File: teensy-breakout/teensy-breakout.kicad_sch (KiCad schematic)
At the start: 80 parts, among them J1 USB_B, J10 Conn_01x04, J11 Conn_01x04, J12 Conn_01x05, J13 Conn_01x03, J14 Conn_01x04, J15 Conn_01x04, J16 1988956, J17 Conn_01x08, J18 Conn_01x08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

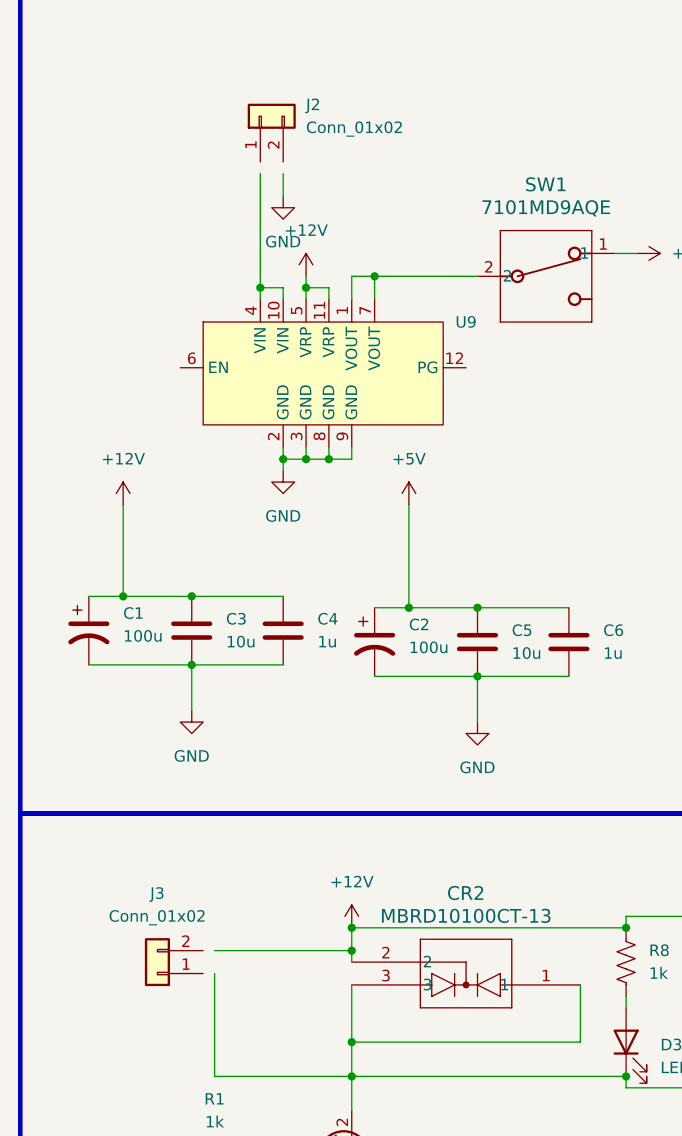
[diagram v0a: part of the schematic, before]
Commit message: Added footprints for connectors. Mostly JST, some XT30 and screw terminals.
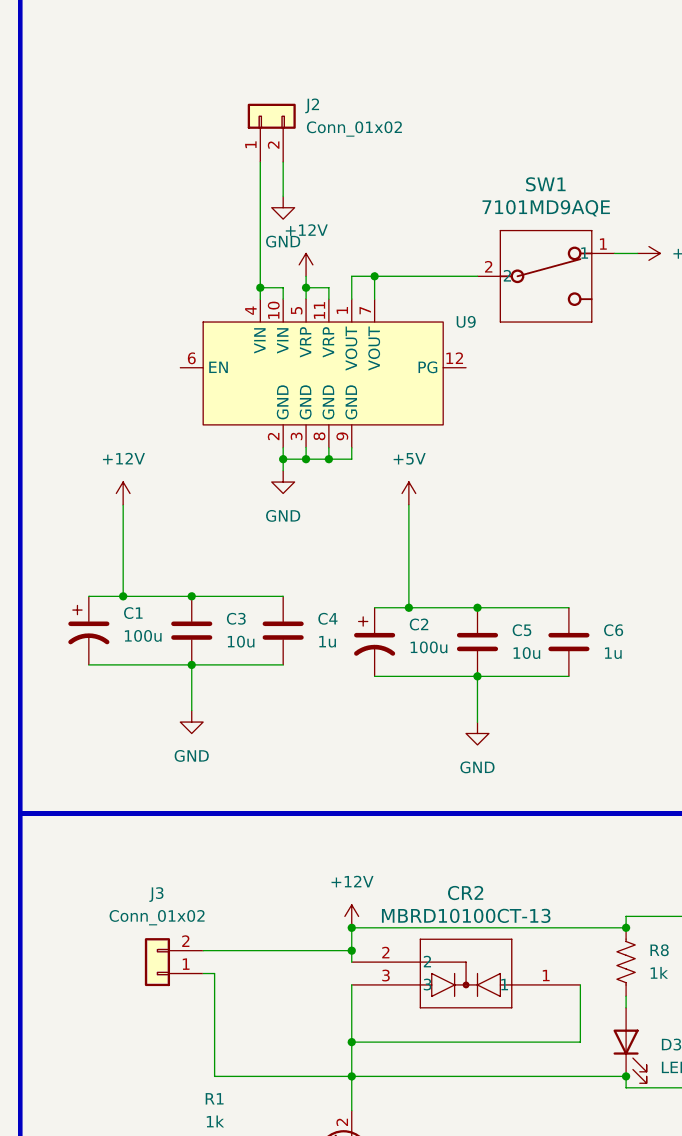
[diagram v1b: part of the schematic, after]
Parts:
- J10, J12, J4, J5, J6, J7, J8, J9: footprint (none) -> Connector_JST:JST_EH_B5B-EH-A_1x05_P2.50mm_Vertical
- J11, J14, J15: footprint (none) -> Connector_JST:JST_EH_B4B-EH-A_1x04_P2.50mm_Vertical
- J13, J19, J20, J21, J22: footprint (none) -> Connector_JST:JST_EH_B3B-EH-A_1x03_P2.50mm_Vertical
- J17, J18: footprint (none) -> Custom:PHOENIX_1989010
- J2, J3: footprint (none) -> Connector_AMASS:AMASS_XT60-F_1x02_P7.20mm_Vertical
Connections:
- net +12V: now also J3.2 (Pin_2)
- net GND: now also J2.2 (Pin_2)
- net at CR2.1, CR2.3, D3.1 (K)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: now also J3.1 (Pin_1)
- net at J2.1 (Pin_1): now also U9.10 (VIN), U9.4 (VIN)
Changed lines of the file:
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@@
 	(wire
 		(pts
-			(xy 33.02 121.92) (xy 48.26 121.92)
-		)
-		(stroke
-			(width 0)
-			(type default)
-		)
-	)
-	(wire
-		(pts
 			(xy 46.99 358.14) (xy 46.99 360.68)
 		)
@@
 	(wire
 		(pts
-			(xy 40.64 35.56) (xy 40.64 38.1)
-		)
-		(stroke
-			(width 0)
-			(type default)
-		)
-	)
-	(wire
-		(pts
 			(xy 218.44 299.72) (xy 219.71 299.72)
 		)
@@
 	(wire
 		(pts
+			(xy 31.75 121.92) (xy 48.26 121.92)
+		)
+		(stroke
+			(width 0)
+			(type default)
+		)
+	)
+	(wire
+		(pts
 			(xy 254 177.8) (xy 254 180.34)
 		)
@@
 	(wire
 		(pts
+			(xy 31.75 124.46) (xy 33.02 124.46)
+		)
+		(stroke
+			(width 0)
+			(type default)
+		)
+	)
+	(wire
+		(pts
 			(xy 341.63 190.5) (xy 350.52 190.5)
 		)
@@
 	(wire
 		(pts
+			(xy 40.64 34.29) (xy 40.64 38.1)
+		)
+		(stroke
+			(width 0)
+			(type default)
+		)
+	)
+	(wire
+		(pts
 			(xy 224.79 36.83) (xy 224.79 21.59)
 		)
@@
 	(wire
 		(pts
-			(xy 38.1 35.56) (xy 38.1 48.26)
+			(xy 38.1 34.29) (xy 38.1 48.26)
 		)
 		(stroke
@@
 			)
 		)
-		(property "Footprint" ""
+		(property "Footprint" "Connector_AMASS:AMASS_XT60-F_1x02_P7.20mm_Vertical"
 			(at 38.1 29.21 0)
 			(effects
@@
 			)
 		)
-		(property "Footprint" ""
+		(property "Footprint" "Connector_JST:JST_EH_B5B-EH-A_1x05_P2.50mm_Vertical"
 			(at 22.86 207.01 0)
 			(effects
@@
 			)
 		)
-		(property "Footprint" ""
+		(property "Footprint" "Connector_JST:JST_EH_B3B-EH-A_1x03_P2.50mm_Vertical"
 			(at 224.79 302.26 0)
 			(effects
@@
 			)
 		)
-		(property "Footprint" ""
+		(property "Footprint" "Connector_JST:JST_EH_B5B-EH-A_1x05_P2.50mm_Vertical"
 			(at 50.8 228.6 0)
 			(effects
@@
 			)
 		)
-		(property "Footprint" ""
+		(property "Footprint" "Connector_JST:JST_EH_B3B-EH-A_1x03_P2.50mm_Vertical"
 			(at 224.79 342.9 0)
 			(effects
@@
 			)
 		)
-		(property "Footprint" ""
+		(property "Footprint" "Custom:PHOENIX_1989010"
 			(at 306.07 81.28 0)
 			(effects
@@
 			)
 		)
-		(property "Footprint" ""
+		(property "Footprint" "Connector_JST:JST_EH_B5B-EH-A_1x05_P2.50mm_Vertical"
 			(at 22.86 184.15 0)
 			(effects
@@
 			)
 		)
-		(property "Footprint" ""
+		(property "Footprint" "Connector_JST:JST_EH_B5B-EH-A_1x05_P2.50mm_Vertical"
 			(at 207.01 182.88 0)
 			(effects
@@
 			)
 		)
-		(property "Footprint" ""
+		(property "Footprint" "Connector_JST:JST_EH_B5B-EH-A_1x05_P2.50mm_Vertical"
 			(at 50.8 207.01 0)
 			(effects
@@
 			)
 		)
-		(property "Footprint" ""
+		(property "Footprint" "Connector_JST:JST_EH_B4B-EH-A_1x04_P2.50mm_Vertical"
 			(at 318.77 60.96 0)
 			(effects
@@
 			)
 		)
-		(property "Footprint" ""
+		(property "Footprint" "Connector_JST:JST_EH_B3B-EH-A_1x03_P2.50mm_Vertical"
 			(at 318.77 35.56 0)
 			(effects
@@
 			)
 		)
-		(property "Footprint" ""
+		(property "Footprint" "Connector_JST:JST_EH_B4B-EH-A_1x04_P2.50mm_Vertical"
 			(at 318.77 48.26 0)
 			(effects
@@
 			)
 		)
-		(property "Footprint" ""
+		(property "Footprint" "Connector_JST:JST_EH_B3B-EH-A_1x03_P2.50mm_Vertical"
 			(at 224.79 322.58 0)
 			(effects
@@
 			)
 		)
-		(property "Footprint" ""
+		(property "Footprint" "Connector_AMASS:AMASS_XT60-F_1x02_P7.20mm_Vertical"
 			(at 26.67 124.46 0)
 			(effects
@@
 			)
 		)
-		(property "Footprint" ""
+		(property "Footprint" "Connector_JST:JST_EH_B5B-EH-A_1x05_P2.50mm_Vertical"
 			(at 106.68 292.1 0)
 			(effects
@@
 			)
 		)
-		(property "Footprint" ""
+		(property "Footprint" "Custom:PHOENIX_1989010"
 			(at 306.07 104.14 0)
 			(effects
@@
 			)
 		)
-		(property "Footprint" ""
+		(property "Footprint" "Connector_JST:JST_EH_B5B-EH-A_1x05_P2.50mm_Vertical"
 			(at 22.86 228.6 0)
 			(effects
@@
 			)
 		)
-		(property "Footprint" ""
+		(property "Footprint" "Connector_JST:JST_EH_B3B-EH-A_1x03_P2.50mm_Vertical"
 			(at 224.79 281.94 0)
 			(effects
@@
 			)
 		)
-		(property "Footprint" ""
+		(property "Footprint" "Connector_JST:JST_EH_B4B-EH-A_1x04_P2.50mm_Vertical"
 			(at 207.01 152.4 0)
 			(effects
@@
 			)
 		)
-		(property "Footprint" ""
+		(property "Footprint" "Connector_JST:JST_EH_B5B-EH-A_1x05_P2.50mm_Vertical"
 			(at 50.8 184.15 0)
 			(effects

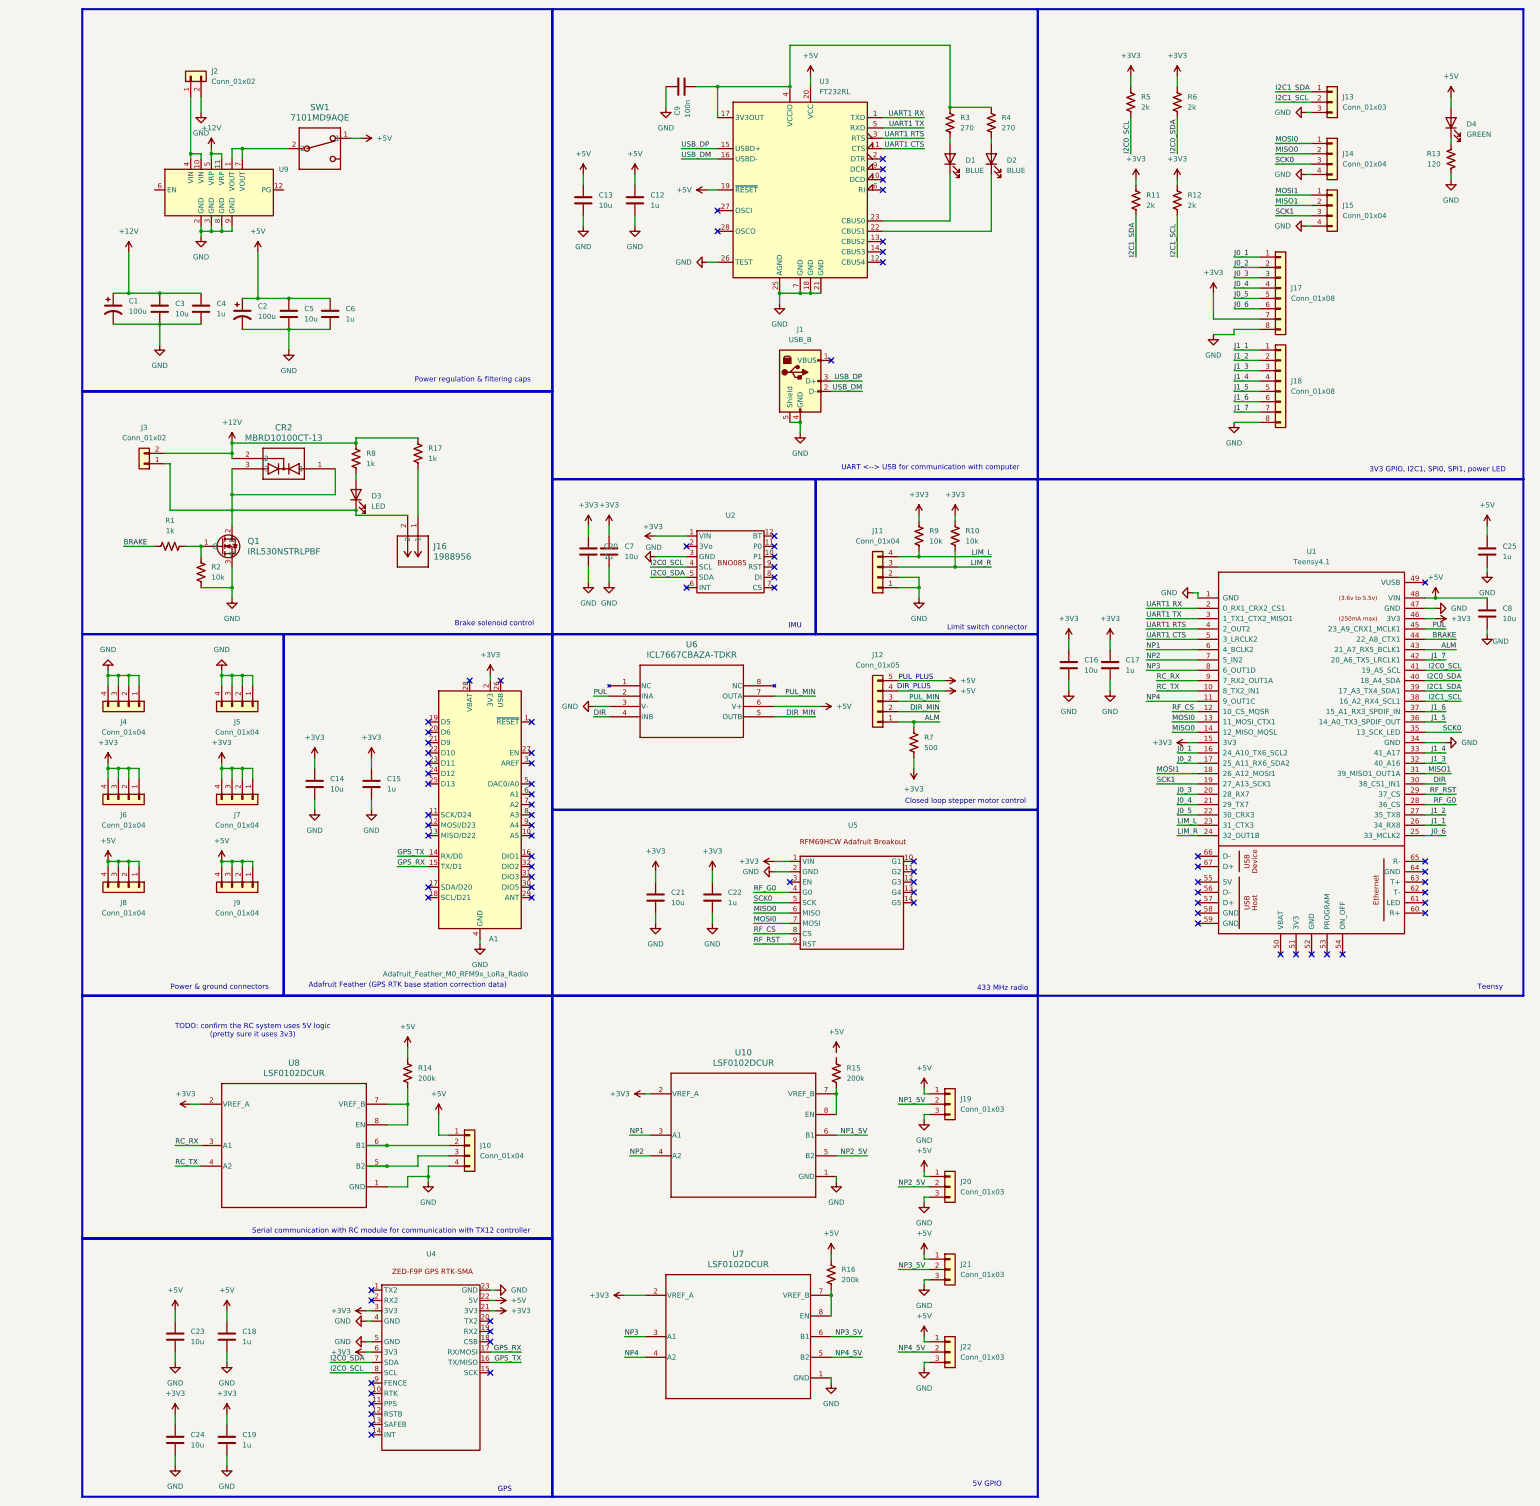
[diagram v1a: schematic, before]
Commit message: Did most of the routing, need to add pinouts and mounting holes
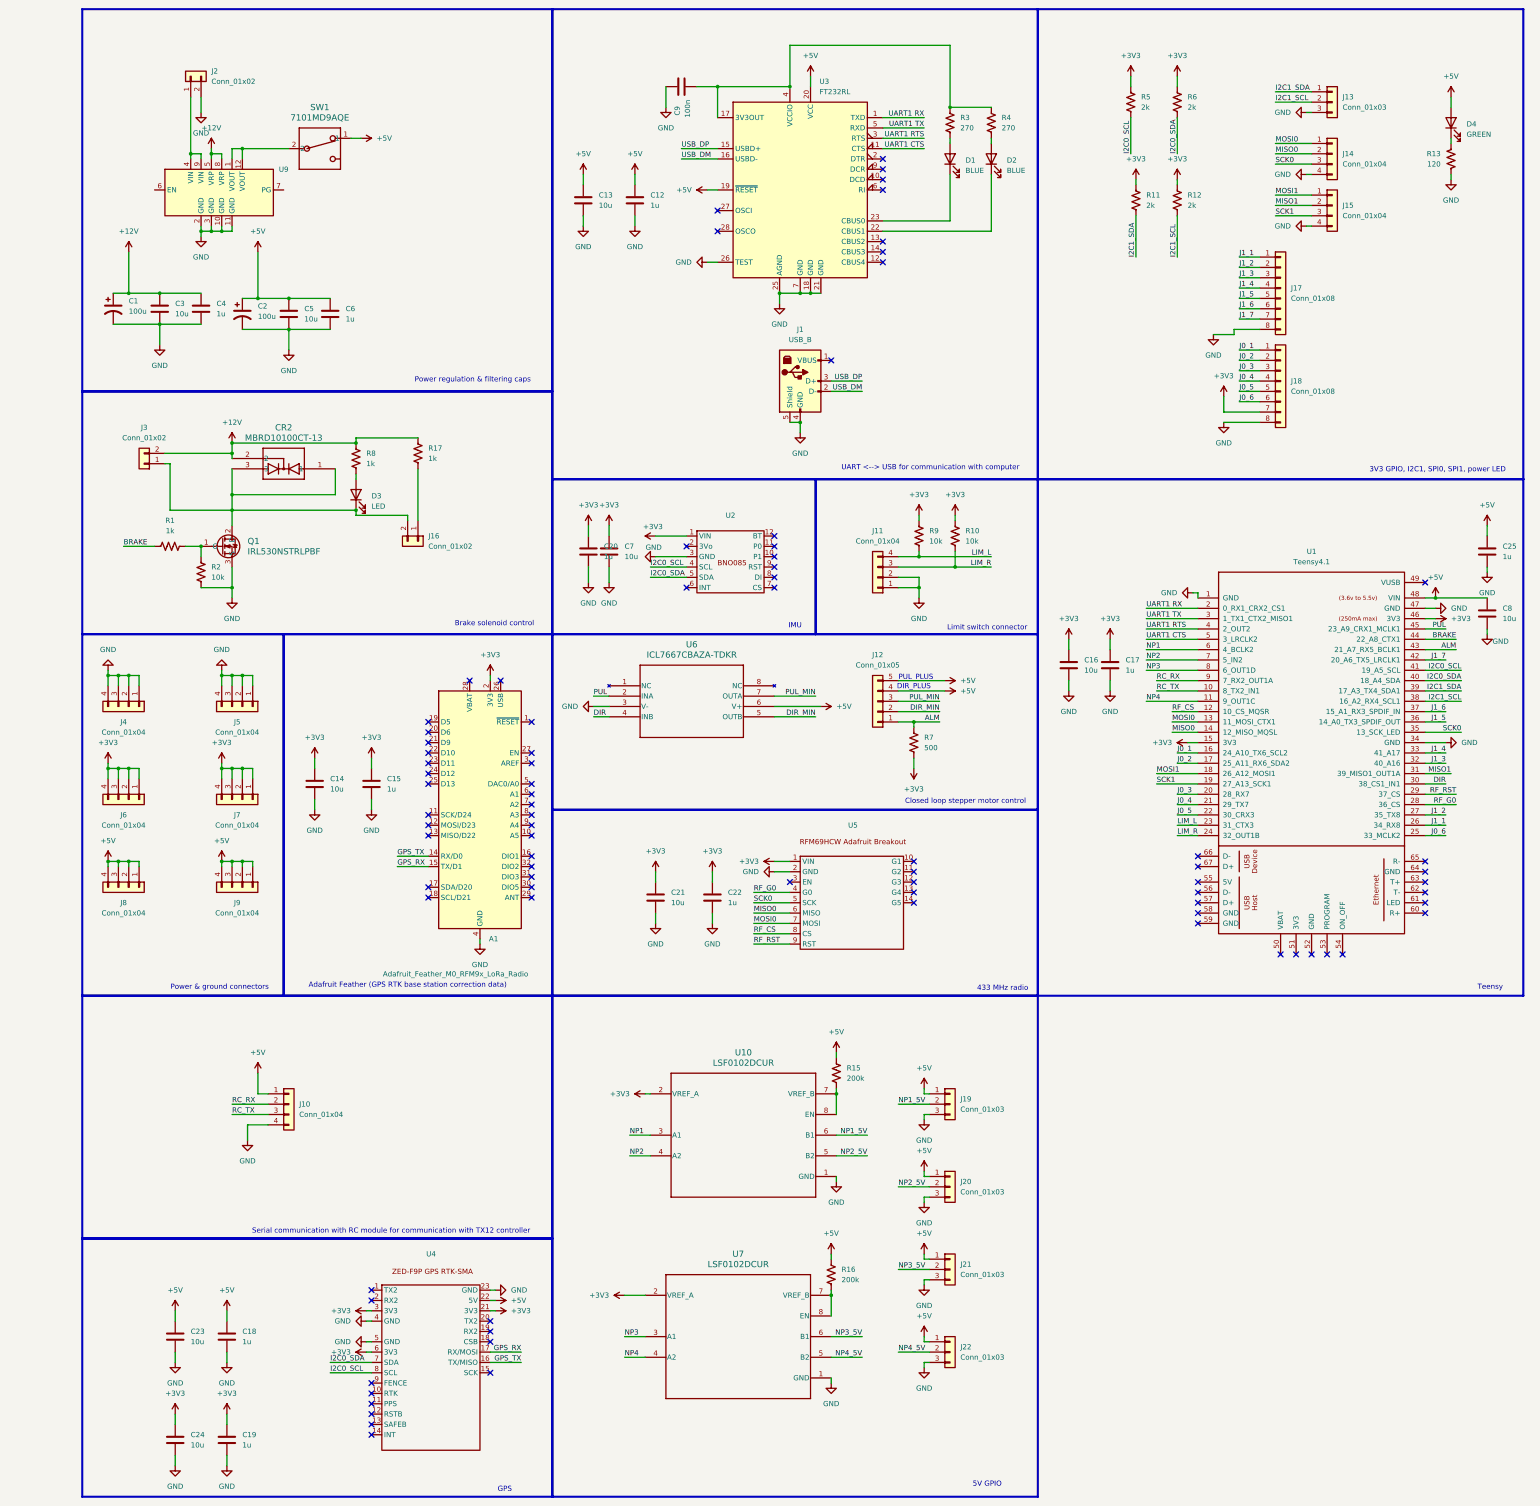
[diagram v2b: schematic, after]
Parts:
- removed J16: 1988956, Custom:CONN_1988956, symbol custom:1988956
- removed R14: 200k, Resistor_SMD:R_0805_2012Metric_Pad1.20x1.40mm_HandSolder, symbol Device:R_US
- removed U8: LSF0102DCUR, DCU0008A_N, symbol custom:LSF0102DCUR
- added J16: Conn_01x02, Connector_JST:JST_EH_B2B-EH-A_1x02_P2.50mm_Vertical, symbol Connector_Generic:Conn_01x02
- J10, J4, J5, J6, J7, J8, J9: footprint Connector_JST:JST_EH_B5B-EH-A_1x05_P2.50mm_Vertical -> Connector_JST:JST_EH_B4B-EH-A_1x04_P2.50mm_Vertical
- U10, U7: footprint DCU0008A_N -> Custom:DCU0008A_M
- U9: footprint (none) -> Custom:Pololu D36V50F5
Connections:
- net +12V: now also U9.8 (VRP); no longer U9.11 (VRP)
- net +3V3: now also J18.7 (Pin_7); no longer J17.7 (Pin_7)
- net +5V: now also R15.1
- net GND: now also U9.10 (GND), U9.11 (GND); no longer U9.8 (GND), U9.9 (GND)
- net J0_1: now also J18.1 (Pin_1); no longer J17.1 (Pin_1)
- net J0_2: now also J18.2 (Pin_2); no longer J17.2 (Pin_2)
- net J0_3: now also J18.3 (Pin_3); no longer J17.3 (Pin_3)
- net J0_4: now also J18.4 (Pin_4); no longer J17.4 (Pin_4)
- net J0_5: now also J18.5 (Pin_5); no longer J17.5 (Pin_5)
- net J0_6: now also J18.6 (Pin_6); no longer J17.6 (Pin_6)
- net J1_1: now also J17.1 (Pin_1); no longer J18.1 (Pin_1)
- net J1_2: now also J17.2 (Pin_2); no longer J18.2 (Pin_2)
- net J1_3: now also J17.3 (Pin_3); no longer J18.3 (Pin_3)
- net J1_4: now also J17.4 (Pin_4); no longer J18.4 (Pin_4)
- net J1_5: now also J17.5 (Pin_5); no longer J18.5 (Pin_5)
- net J1_6: now also J17.6 (Pin_6); no longer J18.6 (Pin_6)
- net J1_7: now also J17.7 (Pin_7); no longer J18.7 (Pin_7)
- net RC_RX: now also J10.2 (Pin_2)
- net RC_TX: now also J10.3 (Pin_3)
- net at R17.2: now also J16.1 (Pin_1)
- net at CR2.1, CR2.3, D3.1 (K)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: now also J16.2 (Pin_2)
- net at J2.1 (Pin_1), U9.4 (VIN): now also U9.9 (VIN); no longer U9.10 (VIN)
- net at SW1.2, U9.1 (VOUT): now also U9.12 (VOUT); no longer U9.7 (VOUT)
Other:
- note removed: "TODO: confirm the RC system uses 5V logic (pretty sure it uses 3v3)"
- moved on the sheet: J10
